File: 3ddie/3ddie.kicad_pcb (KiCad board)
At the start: 2 copper layers, 150 x 170 mm, 54 parts, among them J1 USB4105-GF-A, J2 TRS_MIDI_IN, J3 TRS_MIDI_OUT, U1 W25Q128JV, U2 RP2040, U3 MCP1702T-3302E_CB, U4 MGC3130-I/MQ, U5 MCP1416R, U6 6N137, Y1 12MHz

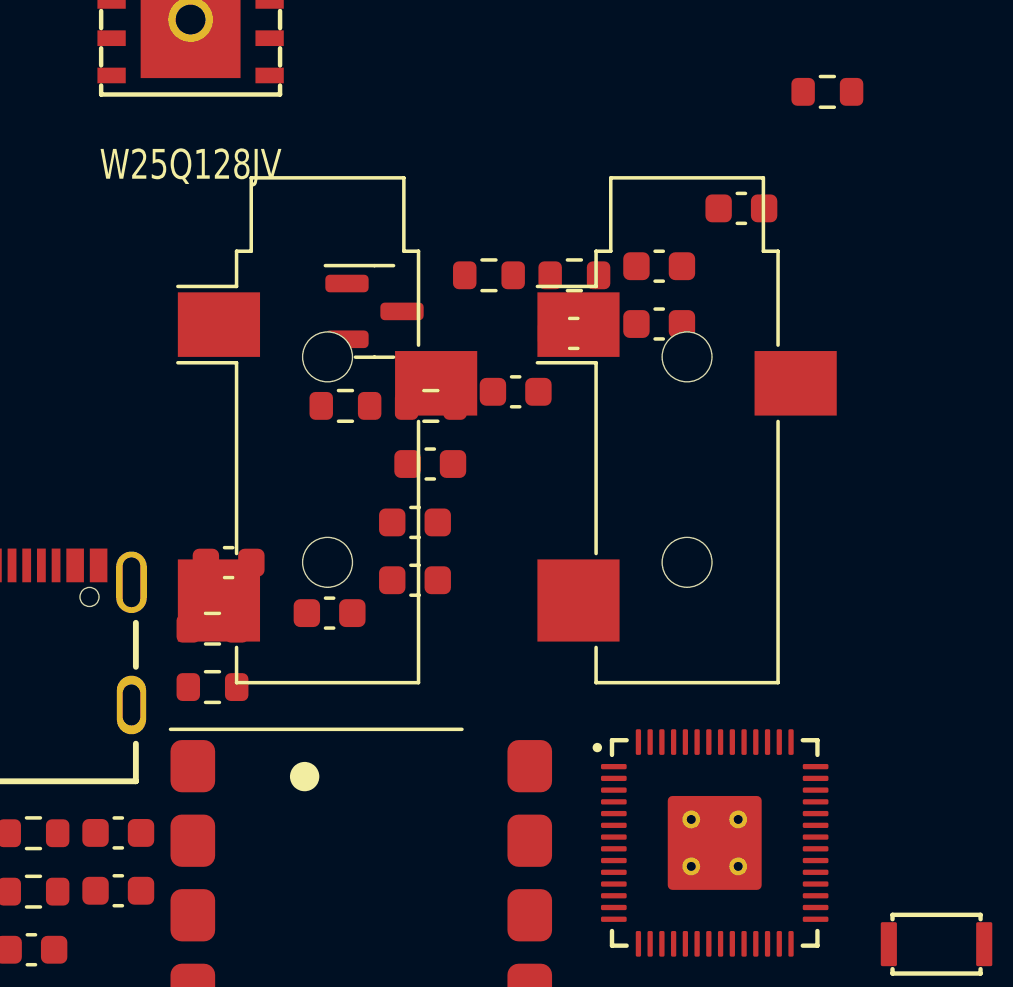
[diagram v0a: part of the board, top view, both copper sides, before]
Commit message: switch to through hole mounting trs jacks
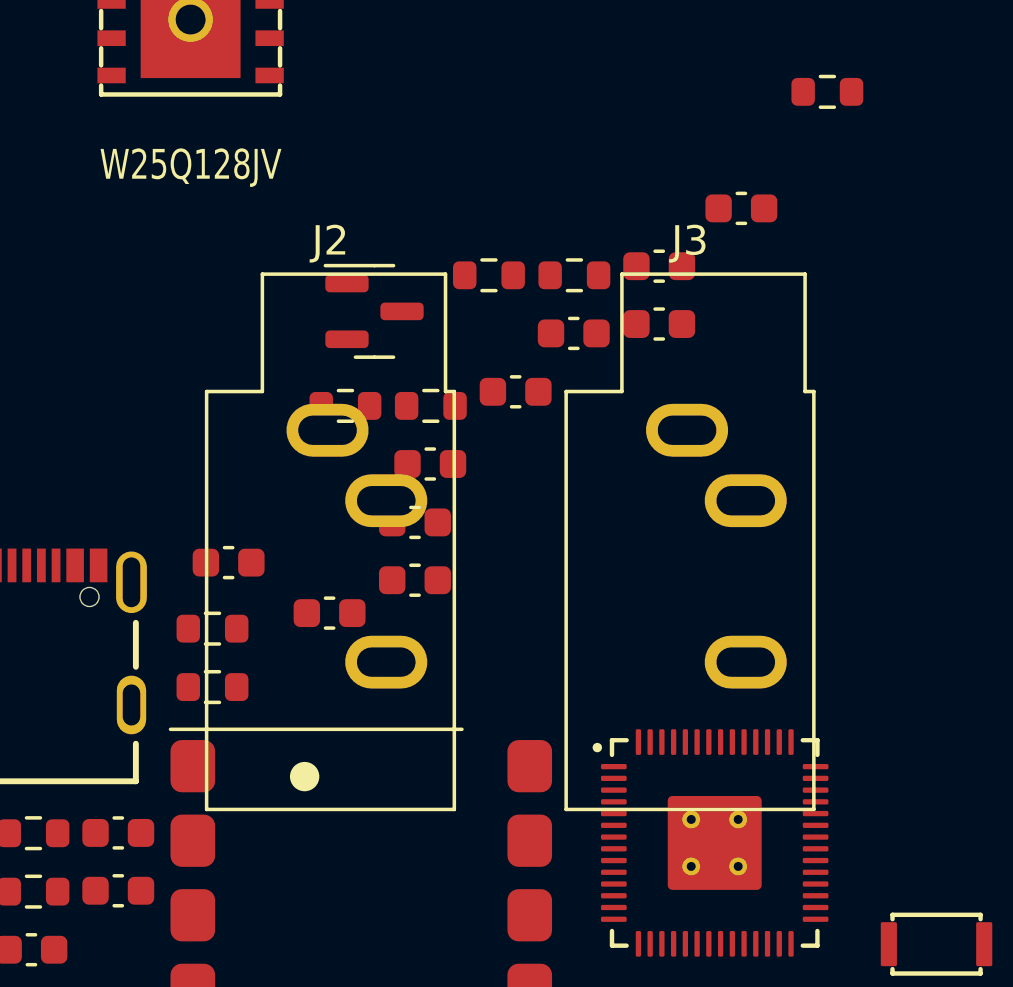
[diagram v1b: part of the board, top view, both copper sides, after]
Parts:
- J2, J3: footprint Connector_Audio:Jack_3.5mm_CUI_SJ-3523-SMT_Horizontal -> Connector_Audio:Jack_3.5mm_CUI_SJ1-3533NG_Horizontal

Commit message: continue layout
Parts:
- C10, C11, C2, C3, C4, C5, C6, C7, C8, C9: footprint Capacitor_SMD:C_0603_1608Metric -> Capacitor_SMD:C_0402_1005Metric
- R5, R6: footprint Resistor_SMD:R_0603_1608Metric -> Resistor_SMD:R_0402_1005Metric
- moved R12 179.2 mm to (149.7, 16.6)
- moved C8 165.1 mm to (136.7, 29.3), turned to 90 degrees
- moved D2 164.2 mm to (149.8, 19.3)
- moved D1 162.0 mm to (143.0, 18.7)
- moved C10 158.4 mm to (133.8, 40.4), turned to -90 degrees
- moved R15 156.7 mm to (128.8, 19.8)
- moved R14 156.6 mm to (128.9, 16.8)
- moved C5 155.6 mm to (138.3, 35.8)
- moved C6 152.7 mm to (138.3, 31.8)
- moved C2 152.6 mm to (127.7, 32.2), turned to 180 degrees
- moved R7 151.1 mm to (142.8, 16.2)
- moved C9 150.2 mm to (135.7, 29.3), turned to 90 degrees
- moved U1 144.5 mm to (120.3, 40.3)
- moved S1 143.8 mm to (118.6, 16.1)
- moved C4 139.7 mm to (132.8, 40.4), turned to -90 degrees
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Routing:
- net +3V3: track 0.00 -> 13.5 mm
- net /5V_TX: track 40.3 -> 34.1 mm
- net Net-(C10-Pad1): track 0.00 -> 5.76 mm
- net GND: track 21.4 -> 19.1 mm
- net Net-(R5-Pad2): track 0.00 -> 1.68 mm
- net Net-(R6-Pad2): track 0.00 -> 1.68 mm
- net Net-(U4-Pad25): track 3.84 -> 2.58 mm
- net Net-(C14-Pad2): track 3.04 -> 3.85 mm
- net /Electrode_RX3: track 13.6 -> 14.2 mm

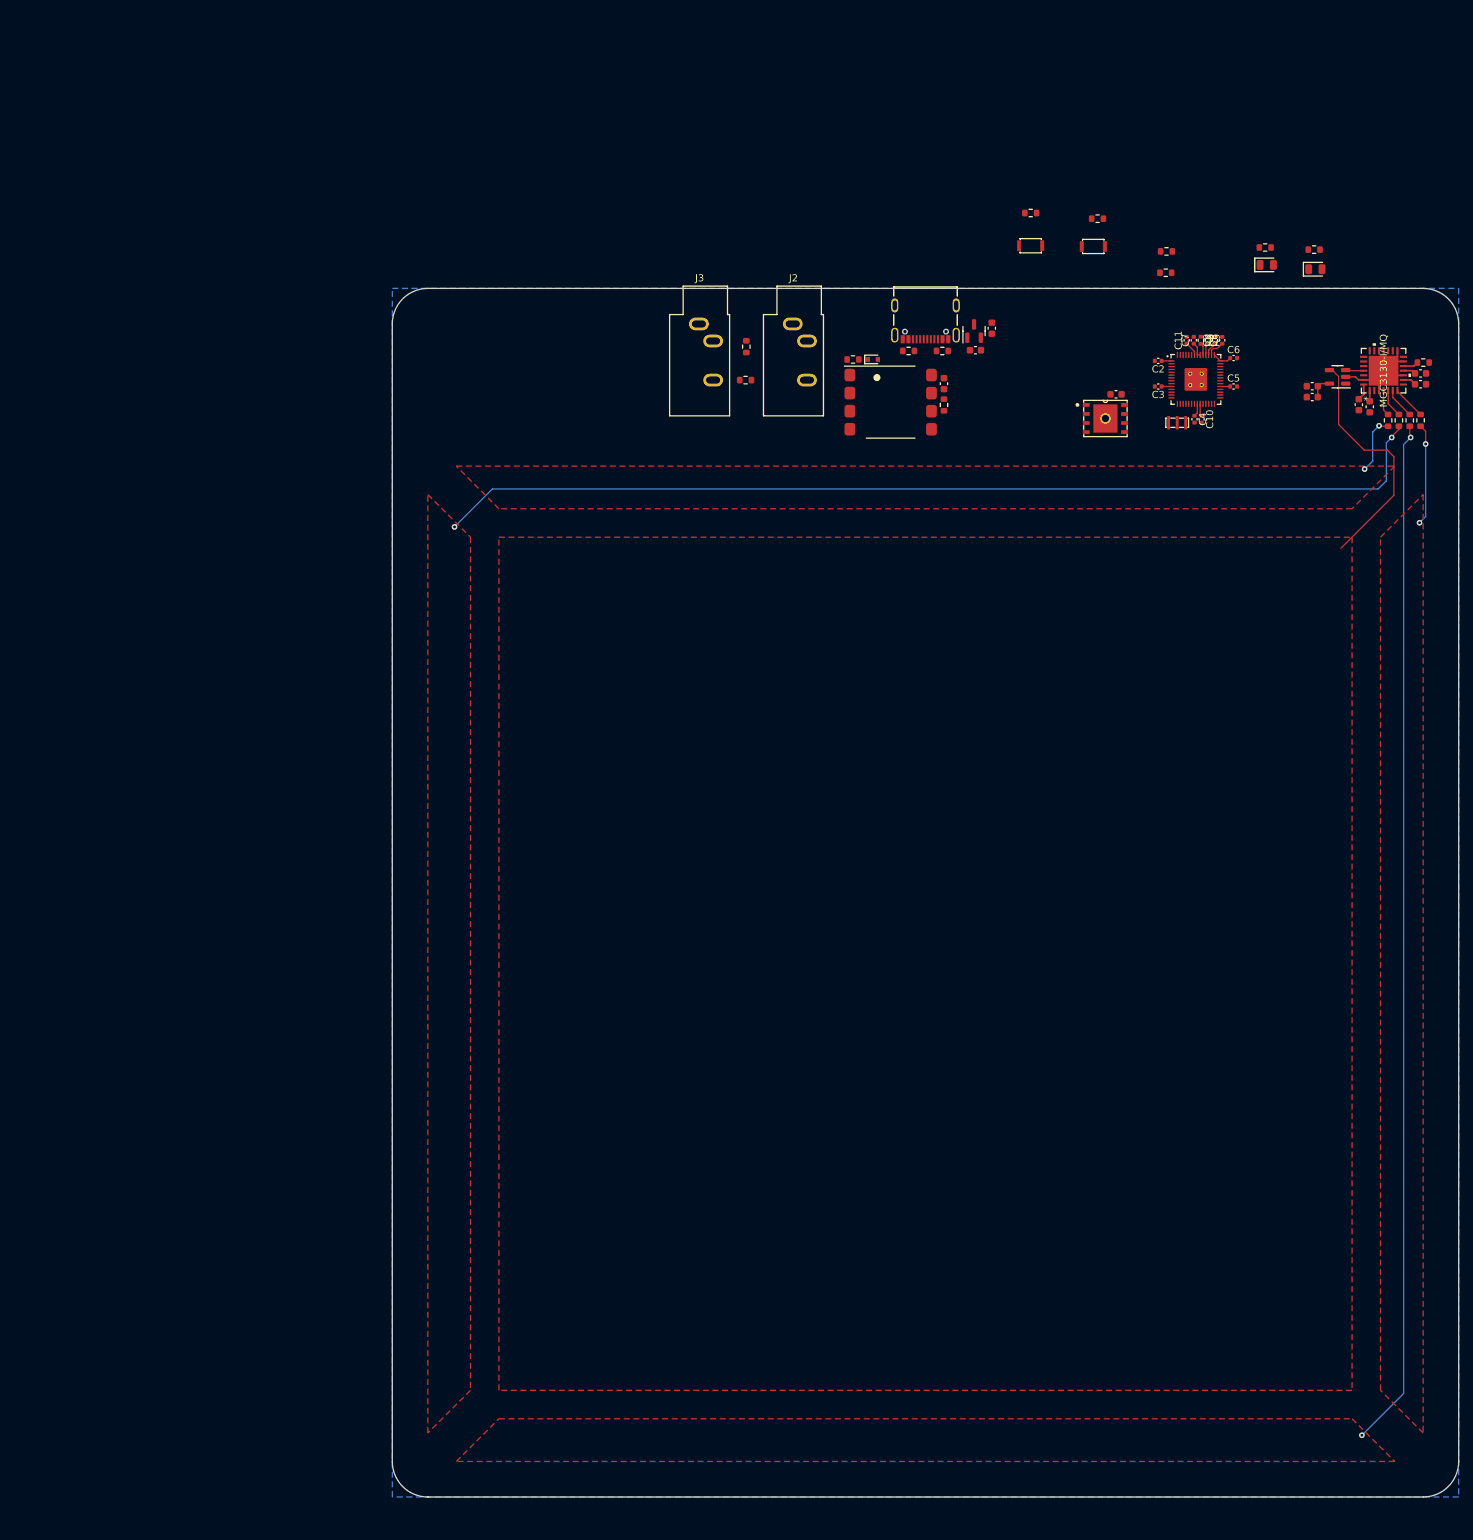
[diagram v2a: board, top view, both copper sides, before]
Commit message: expand board outline, add dimensions
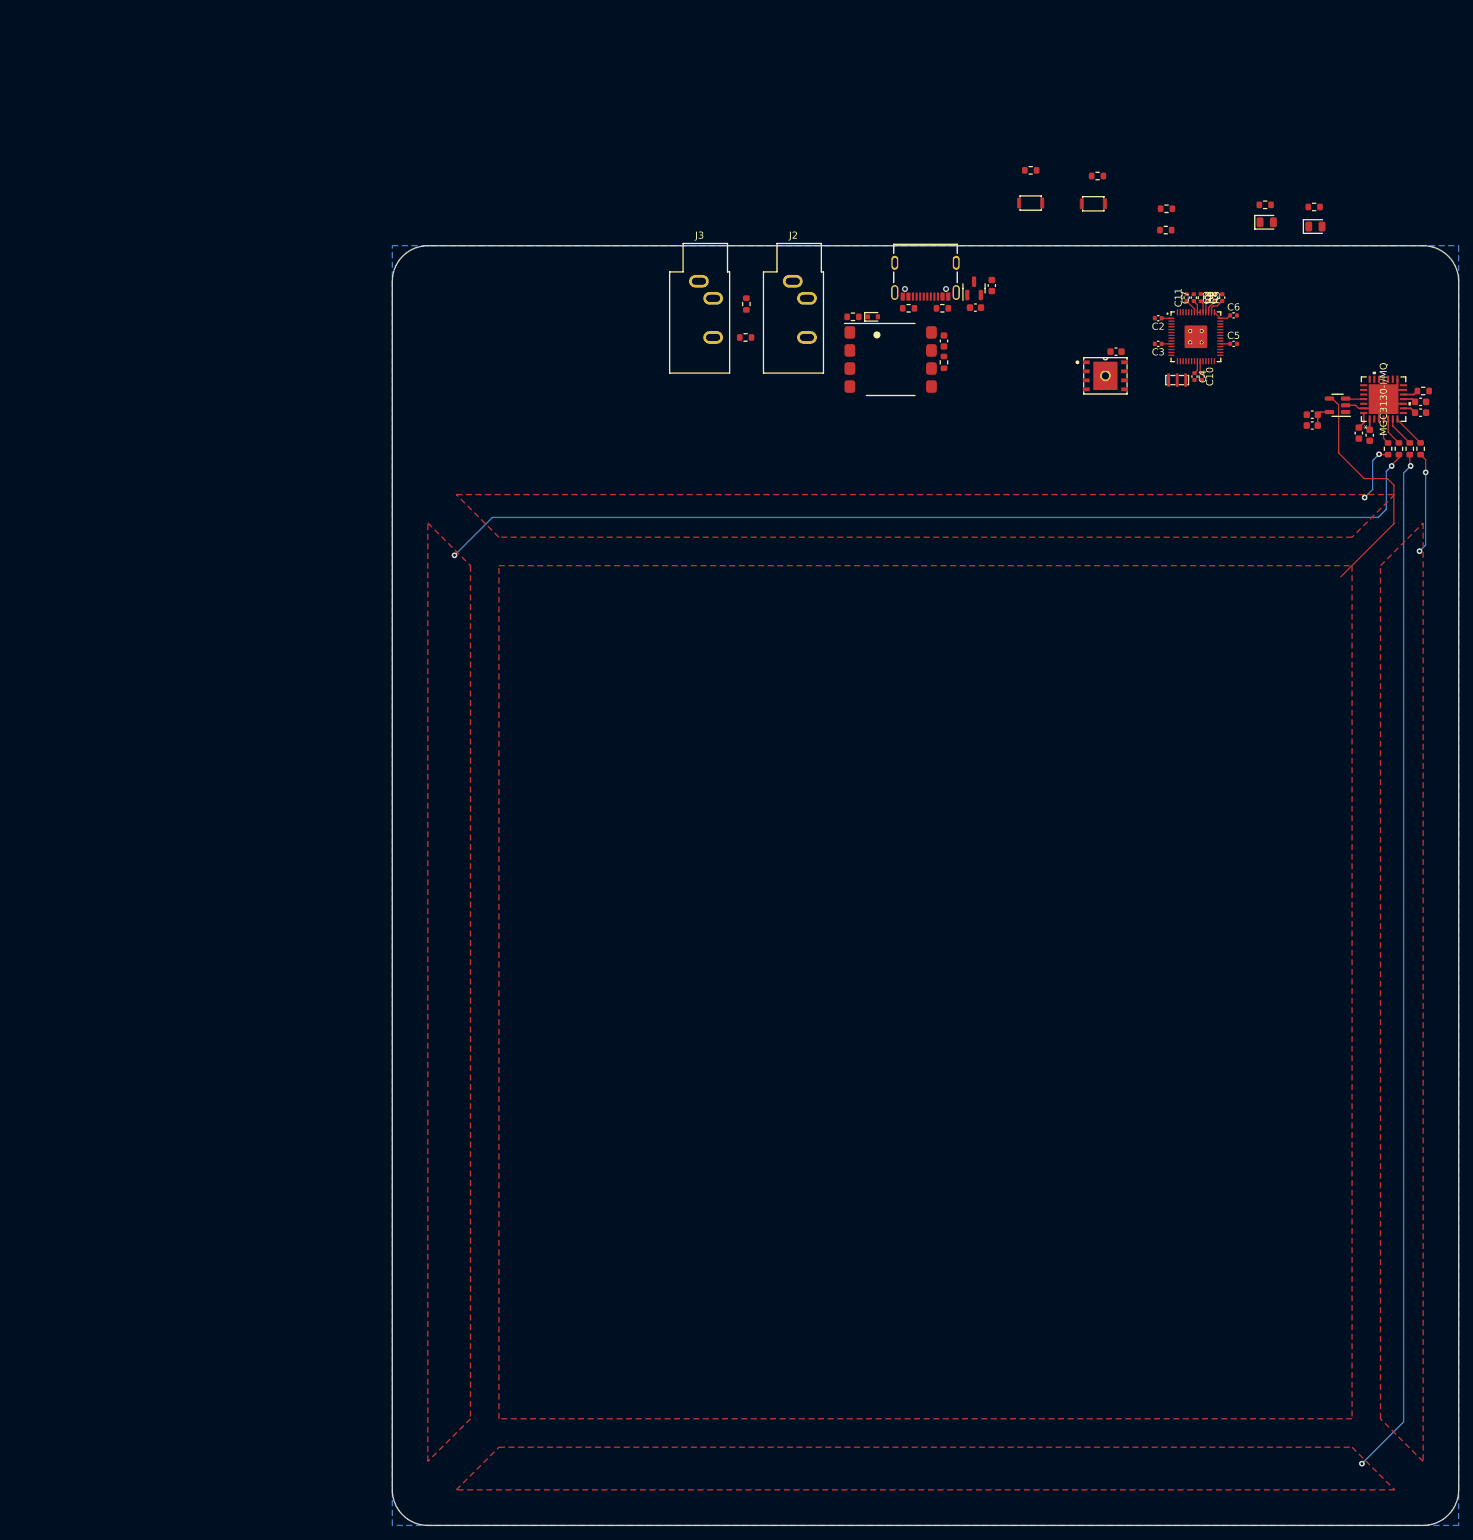
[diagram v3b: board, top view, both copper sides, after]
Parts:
- moved C2 6.00 mm to (127.7, 26.2)
- moved S1 6.00 mm to (118.6, 10.1)
- moved C1 6.00 mm to (121.8, 30.9)
- moved C10 6.00 mm to (133.8, 34.4)
- moved C11 6.00 mm to (131.7, 23.3)
- moved C12 6.00 mm to (104.3, 21.6)
- moved C13 6.00 mm to (102.0, 24.7)
- moved C18 6.00 mm to (97.6, 29.4)
- moved C4 6.00 mm to (132.8, 34.4)
- moved C6 6.00 mm to (138.3, 25.8)
- moved C7 6.00 mm to (132.7, 23.3)
- moved C8 6.00 mm to (136.7, 23.3)
- moved C9 6.00 mm to (135.7, 23.3)
- moved D1 6.00 mm to (143.0, 12.7)
- moved D2 6.00 mm to (149.8, 13.3)
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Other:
- board size 150 x 170 mm -> 150 x 180 mm

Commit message: continued routing
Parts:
- added J4: Conn_02x11_Counter_Clockwise, Connector_PinSocket_2.54mm:PinSocket_2x11_P2.54mm_Horizontal, F.Cu at (148.6, -3.88)
- added RV1: 10K, 3ddie:PDB12-H4251-103BF, F.Cu at (57.3, 8.20)
- added RV2: 10K, 3ddie:PDB12-H4251-103BF, F.Cu at (42.0, 8.20)
- moved J1 55.0 mm to (150.0, 18.4)
- moved R1 55.0 mm to (147.6, 24.8)
- moved R4 55.0 mm to (152.4, 24.8)
- moved C13 39.8 mm to (141.8, 25.9)
- moved C12 39.8 mm to (144.1, 22.8)
- moved U3 39.8 mm to (141.6, 23.2)
- moved R14 31.0 mm to (126.1, 41.7), turned to -90 degrees
- moved R15 27.9 mm to (127.6, 41.7), turned to -90 degrees
- moved R17 20.4 mm to (89.9, 27.4), turned to 0 degrees
- moved R18 20.2 mm to (89.9, 28.9)
- moved C18 20.0 mm to (117.6, 29.4)
- moved D3 20.0 mm to (107.6, 26.0)
- moved J2 20.0 mm to (96.3, 21.0)
- moved R16 20.0 mm to (104.8, 26.0)
- moved R19 20.0 mm to (117.6, 32.4)
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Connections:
- net Net-(J1-PadA6) renamed /D+
- net Net-(J1-PadA7) renamed /D-
- U2 pad 38: /GPIO26 -> /POT1
- U2 pad 39: /GPIO27 -> /POT2
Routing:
- net /VBUS: track 3.32 -> 36.4 mm
- net /D+: track 0.00 -> 21.4 mm
- net /D-: track 0.00 -> 21.0 mm
- net Net-(D3-Pad2): track 0.00 -> 19.9 mm
- net Net-(U1-Pad7): track 0.00 -> 14.0 mm
- net Net-(U1-Pad6): track 0.00 -> 12.6 mm
- net /BOOT: track 0.00 -> 11.6 mm
- net Net-(U1-Pad2): track 0.00 -> 10.2 mm
- net Net-(U1-Pad5): track 0.00 -> 10.2 mm
- net Net-(U1-Pad3): track 0.00 -> 9.23 mm
- net Net-(J2-PadR): track 0.00 -> 7.10 mm
- net Net-(D3-Pad1): track 0.00 -> 6.53 mm
- net /EIO4/SI0: track 0.00 -> 6.34 mm
- net Net-(J3-PadT): track 0.00 -> 5.63 mm
- net /EIO5/SI1: track 0.00 -> 5.49 mm
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
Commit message: layout and schema changes
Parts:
- J4: value Conn_02x11_Counter_Clockwise -> Conn_02x15_Odd_Even; footprint Connector_PinSocket_2.54mm:PinSocket_2x11_P2.54mm_Horizontal -> Connector_IDC:IDC-Header_2x15_P2.54mm_Horizontal
- moved J4 61.5 mm to (97.1, 29.7), turned to 90 degrees
- moved RV2 21.3 mm to (34.0, 27.9)
- moved RV1 19.6 mm to (57.5, 27.8)
- moved R17 18.6 mm to (73.0, 35.2)
- moved C12 15.5 mm to (159.6, 22.0)
- moved D2 15.5 mm to (157.2, 17.9)
- moved U3 15.5 mm to (157.1, 22.4)
- moved C13 15.5 mm to (157.3, 25.1)
- moved R12 15.5 mm to (157.2, 19.7)
- moved R18 15.1 mm to (76.2, 35.2)
- moved U6 12.8 mm to (99.2, 38.8)
- moved C18 12.7 mm to (106.9, 36.1)
- moved R19 12.7 mm to (106.9, 39.1)
- moved R16 12.6 mm to (94.2, 32.8)
- moved D3 12.4 mm to (97.2, 32.8)
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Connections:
- J4 pad 1: /GPIO2 -> GND
- J4 pad 10: /GPIO11 -> /GPIO26
- J4 pad 11: /GPIO15 -> /GPIO24
- J4 pad 12: /GPIO16 -> /GPIO23
- J4 pad 13: /GPIO17 -> /GPIO22
- J4 pad 14: /GPIO18 -> /GPIO21
- J4 pad 15: /GPIO19 -> /GPIO20
- J4 pad 16: /GPIO20 -> /GPIO19
- J4 pad 17: /GPIO21 -> /GPIO18
- J4 pad 18: /GPIO22 -> /GPIO17
- J4 pad 19: /GPIO23 -> /GPIO16
- J4 pad 2: /GPIO3 -> +3V3
- J4 pad 20: /GPIO24 -> /GPIO15
- J4 pad 21: /GPIO28 -> /GPIO11
- J4 pad 22: /GPIO29 -> /GPIO10
- J4 pad 3: /GPIO4 -> GND
- J4 pad 4: /GPIO5 -> +3V3
- J4 pad 5: /GPIO6 -> /BOOT
- J4 pad 6: /GPIO7 -> /VBUS
- J4 pad 7: /GPIO8 -> /RUN
- J4 pad 8: /GPIO9 -> /VBUS
- J4 pad 9: /GPIO10 -> /GPIO27
- U2 pad 38: /POT1 -> /GPIO26
- U2 pad 39: /POT2 -> /GPIO27
- U2 pad 40: /GPIO28 -> /POT1
- U2 pad 41: /GPIO29 -> /POT2
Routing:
- net /GPIO26: track 0.00 -> 56.8 mm
- net /GPIO27: track 0.00 -> 56.0 mm
- net /GPIO23: track 0.00 -> 52.3 mm
- net /GPIO24: track 0.00 -> 51.6 mm
- net /GPIO22: track 0.00 -> 45.9 mm
- net /GPIO21: track 0.00 -> 43.7 mm
- net /GPIO19: track 0.00 -> 39.3 mm
- net /GPIO20: track 0.00 -> 38.3 mm
- net /GPIO17: track 0.00 -> 34.1 mm
- net /GPIO18: track 0.00 -> 33.5 mm
- net /POT1: track 0.00 -> 32.3 mm
- net /GPIO16: track 0.00 -> 29.6 mm
- net /GPIO15: track 0.00 -> 28.2 mm
- net /GPIO10: track 0.00 -> 17.0 mm
- net /GPIO8: track 0.00 -> 15.1 mm
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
